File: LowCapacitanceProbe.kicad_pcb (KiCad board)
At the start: 2 copper layers, 23 x 15 mm, 21 parts, among them J1 u.Fl, J5 u.Fl, Q1 BF998, U1 SPX3819M5-L

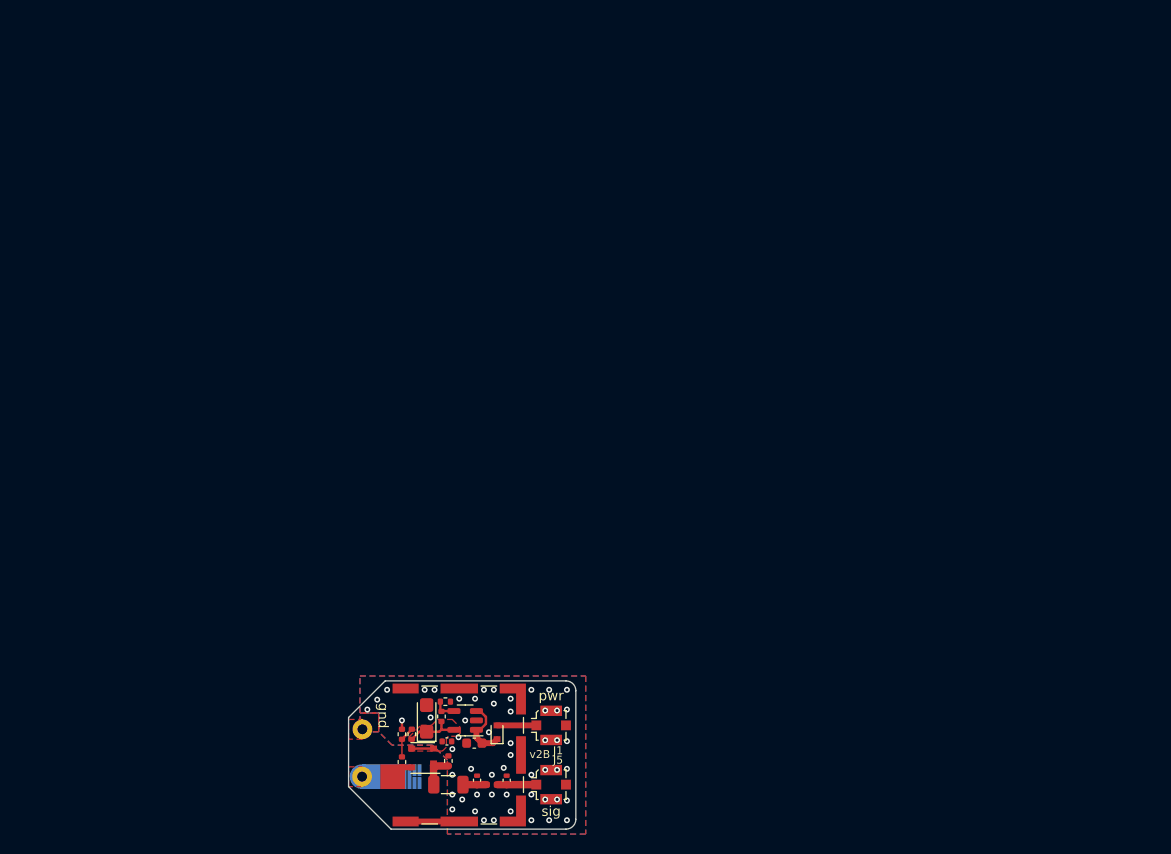
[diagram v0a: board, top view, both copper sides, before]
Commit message: Added net labels, synchronised PCB with SCH, grouped all elements.
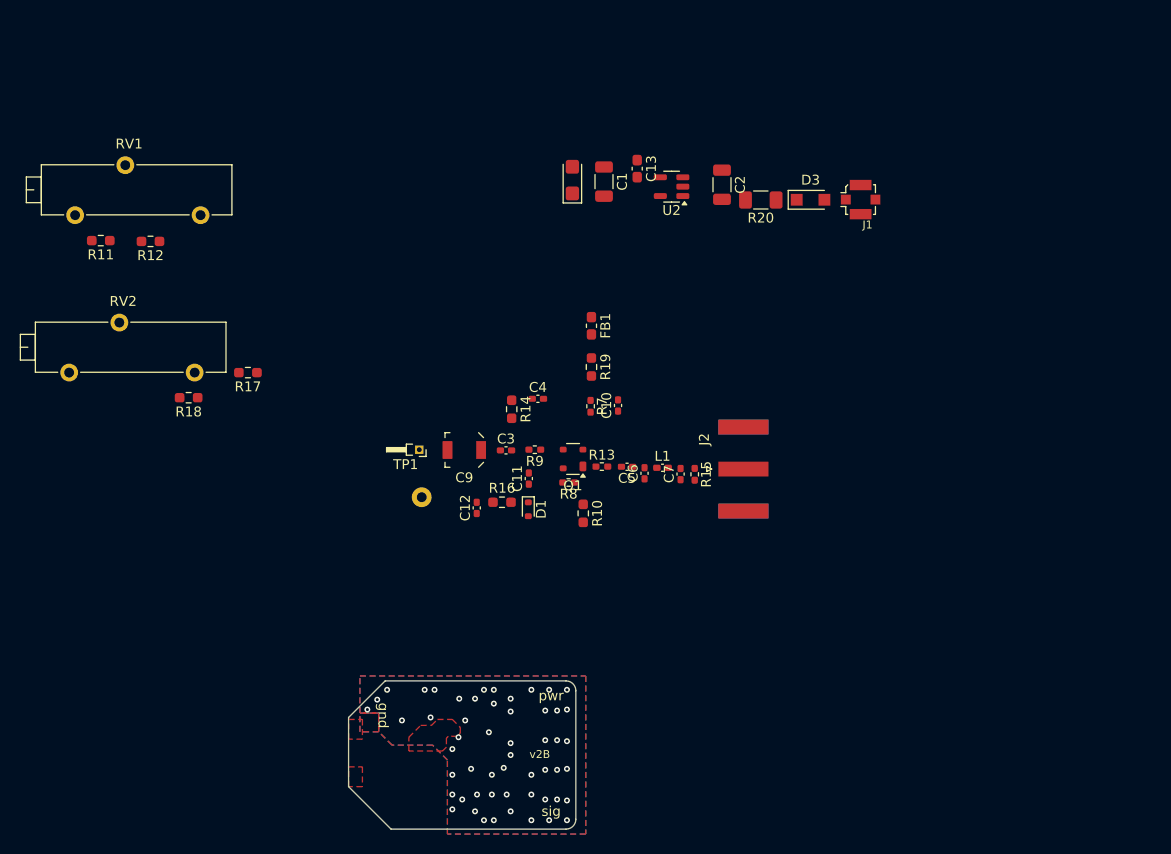
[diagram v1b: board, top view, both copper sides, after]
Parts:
- removed D2: NSR0520V2T1G, Diode_SMD:D_SOD-523
- removed J5: u.Fl, Connector_Coaxial:U.FL_Molex_MCRF_73412-0110_Vertical
- removed N1: Laird_BMI-S-101, RF_Shielding:Laird_Technologies_BMI-S-101_13.66x12.70mm
- removed R1: 4k7, Resistor_SMD:R_0402_1005Metric
- removed R2: 5k6, Resistor_SMD:R_0402_1005Metric
- removed R3: 1M, Resistor_SMD:R_0402_1005Metric
- removed R4: 47R, Resistor_SMD:R_0402_1005Metric
- removed R5: 27k, Resistor_SMD:R_0402_1005Metric
- removed R6: 12k, Resistor_SMD:R_0402_1005Metric
- removed U1: SPX3819M5-L, Package_TO_SOT_SMD:SOT-23-5
- added C10: 100n, Capacitor_SMD:C_0402_1005Metric_Pad0.74x0.62mm_HandSolder, F.Cu at (129.3, 64.6)
- added C11: 3p, Capacitor_SMD:C_0402_1005Metric_Pad0.74x0.62mm_HandSolder, F.Cu at (120.2, 72.0)
- added C12: 100n, Capacitor_SMD:C_0402_1005Metric_Pad0.74x0.62mm_HandSolder, F.Cu at (115.0, 75.0)
- added C13: 100n, Capacitor_SMD:C_0603_1608Metric_Pad1.08x0.95mm_HandSolder, F.Cu at (131.2, 40.7)
- added C3: 3p, Capacitor_SMD:C_0402_1005Metric_Pad0.74x0.62mm_HandSolder, F.Cu at (117.9, 69.2)
- added C9: 1.5-3p, Capacitor_SMD:C_Trimmer_Voltronics_JR, F.Cu at (113.7, 69.1)
- added D1: SMV1232, Diode_SMD:D_SOD-523, F.Cu at (120.2, 75.1)
- added D3: PMEG4020ER, Diode_SMD:Nexperia_CFP3_SOD-123W, F.Cu at (148.8, 43.8)
- added FB1: 0R, Inductor_SMD:L_0603_1608Metric_Pad1.05x0.95mm_HandSolder, F.Cu at (126.6, 56.6)
- added J2: SMA, Connector_Coaxial:SMA_Amphenol_132289_EdgeMount, F.Cu at (142.0, 71.1)
- added R10: 75, Resistor_SMD:R_0603_1608Metric_Pad0.98x0.95mm_HandSolder, F.Cu at (125.8, 75.5)
- added R11: 2k, Resistor_SMD:R_0603_1608Metric_Pad0.98x0.95mm_HandSolder, F.Cu at (76.9, 47.9)
- added R12: 2k, Resistor_SMD:R_0603_1608Metric_Pad0.98x0.95mm_HandSolder, F.Cu at (82.0, 48.0)
- added R13: 0R, Resistor_SMD:R_0402_1005Metric_Pad0.72x0.64mm_HandSolder, F.Cu at (127.6, 70.8)
- added R14: 1M, Resistor_SMD:R_0603_1608Metric_Pad0.98x0.95mm_HandSolder, F.Cu at (118.5, 65.0)
- added R15: 100k, Resistor_SMD:R_0402_1005Metric_Pad0.72x0.64mm_HandSolder, F.Cu at (137.0, 71.6)
- added R16: 1M, Resistor_SMD:R_0603_1608Metric_Pad0.98x0.95mm_HandSolder, F.Cu at (117.5, 74.4)
- added R17: 0R, Resistor_SMD:R_0603_1608Metric_Pad0.98x0.95mm_HandSolder, F.Cu at (91.8, 61.3)
- added R18: 3k, Resistor_SMD:R_0603_1608Metric_Pad0.98x0.95mm_HandSolder, F.Cu at (85.8, 63.8)
- added R19: 0R, Resistor_SMD:R_0603_1608Metric_Pad0.98x0.95mm_HandSolder, F.Cu at (126.6, 60.7)
- added R20: 10, Resistor_SMD:R_1206_3216Metric_Pad1.30x1.75mm_HandSolder, F.Cu at (143.7, 43.8)
- added R7: 10, Resistor_SMD:R_0402_1005Metric_Pad0.72x0.64mm_HandSolder, F.Cu at (126.5, 64.7)
- added R8: 39, Resistor_SMD:R_0402_1005Metric_Pad0.72x0.64mm_HandSolder, F.Cu at (124.3, 72.4)
- added R9: 39, Resistor_SMD:R_0402_1005Metric_Pad0.72x0.64mm_HandSolder, F.Cu at (120.8, 69.1)
- added RV1: 10k, Potentiometer_THT:Potentiometer_Bourns_3006W_Horizontal, F.Cu at (87.0, 45.4)
- added RV2: 10k, Potentiometer_THT:Potentiometer_Bourns_3006W_Horizontal, F.Cu at (86.4, 61.3)
- added TP1: Fixed needle, Connector_PinHeader_1.00mm:PinHeader_1x01_P1.00mm_Horizontal, F.Cu at (109.2, 69.1)
- added U2: SPX3819M5-L-5-0, Package_TO_SOT_SMD:SOT-23-5, F.Cu at (134.7, 42.5)
- C1: footprint Capacitor_SMD:C_0402_1005Metric -> Capacitor_SMD:C_1206_3216Metric
- C2: footprint Capacitor_SMD:C_0603_1608Metric -> Capacitor_SMD:C_1206_3216Metric
- C4: value C -> 100n; footprint FETProbe:input_cap -> Capacitor_SMD:C_0402_1005Metric_Pad0.74x0.62mm_HandSolder
- C5: value 100nF -> 100n; footprint Capacitor_SMD:C_1206_3216Metric -> Capacitor_SMD:C_0402_1005Metric_Pad0.74x0.62mm_HandSolder
- C6, C7: value 2.2pF -> DNP; footprint FETProbe:C_0402_1005Metric_mod -> Capacitor_SMD:C_0402_1005Metric_Pad0.74x0.62mm_HandSolder
- L1: value 10nH -> 4n7; footprint Inductor_SMD:L_0402_1005Metric -> Inductor_SMD:L_0402_1005Metric_Pad0.77x0.64mm_HandSolder
- Q1: footprint FETProbe:SOT-143_mod -> Package_TO_SOT_SMD:SOT-143
- TP3: value TestPoint -> Pogo needle
- moved C2 61.8 mm to (139.8, 42.3), turned to -90 degrees
- moved J1 61.7 mm to (153.8, 43.8)
- moved C1 58.8 mm to (127.8, 42.0), turned to -90 degrees
- moved C8 56.4 mm to (124.7, 41.8)
- moved C4 40.4 mm to (121.2, 64.0)
- moved C5 36.9 mm to (130.2, 70.8), turned to 180 degrees
- moved L1 36.4 mm to (133.8, 70.9)
- moved C7 35.6 mm to (135.6, 71.6), turned to 90 degrees
- moved C6 35.4 mm to (131.9, 71.5), turned to 90 degrees
- moved Q1 33.9 mm to (124.7, 70.0)
- moved TP3 24.2 mm to (109.4, 73.9)
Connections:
- net /out renamed /OUT
- C1 pad 2: 4V0 -> +5V
- C2 pad 2: Net-(D2-K) -> /PIN_FILT
- C4 pad 1: unconnected-(C4-Pad1) -> /G2_BIAS
- C4 pad 2: Net-(Q1-G1) -> GND
- C5 pad 1: /out2 -> /OUT_UNF
- C5 pad 2: /out1 -> Net-(C5-Pad2)
- C6 pad 2: /out1 -> /OUT_UNF
- C8 pad 1: 4V0 -> +5V
- J1 pad 1: Net-(D2-A) -> /PIN
- L1 pad 1: /out1 -> /OUT_UNF
- Q1 pad 1: /out2 -> /SOURCE
- Q1 pad 2: 4V0 -> /DRAIN
- Q1 pad 3: 4V0 -> /G2
- Q1 pad 4: Net-(Q1-G1) -> /G1
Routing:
- net 4V0: track 7.69 -> 0.00 mm
- net Net-(D2-K): track 6.40 -> 0.00 mm
- net GND: track 5.81 -> 0.00 mm
- net Net-(D2-A): track 3.97 -> 0.00 mm
- net /OUT: track 3.92 -> 0.00 mm
- net /out2: track 3.49 -> 0.00 mm
- net Net-(R1-Pad2): track 3.21 -> 0.00 mm
- net /out1: track 2.35 -> 0.00 mm
- net Net-(U1-ADJ): track 2.31 -> 0.00 mm
- net Net-(Q1-G1): track 0.96 -> 0.00 mm
- added copper zone on F.Cu, net (none)
- added copper zone on F.Cu, net +5V
- removed copper zone on F.Cu, net 4V0
- removed copper zone on F.Cu, net unconnected-(C4-Pad1)

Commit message: Slight fixes, simulation modified for varicap analysis and noise analysis, started routing of PCB.
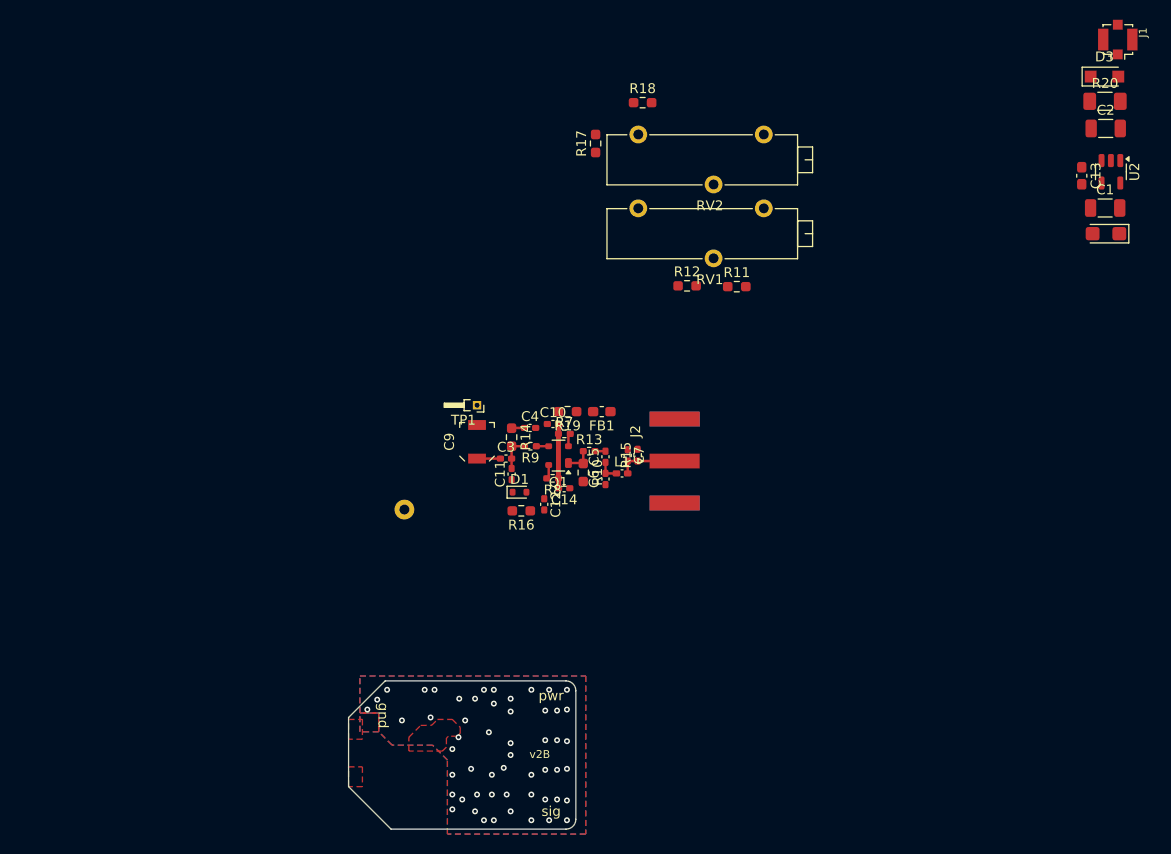
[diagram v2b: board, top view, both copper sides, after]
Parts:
- added C14: 100n, Capacitor_SMD:C_0402_1005Metric_Pad0.74x0.62mm_HandSolder, F.Cu at (123.8, 73.0)
- moved R11 64.5 mm to (141.3, 52.6), turned to 0 degrees
- moved R18 54.8 mm to (131.8, 34.0), turned to 0 degrees
- moved R12 54.5 mm to (136.3, 52.5), turned to 0 degrees
- moved C8 54.3 mm to (178.7, 47.2), turned to 180 degrees
- moved RV2 51.0 mm to (131.3, 37.2), turned to 180 degrees
- moved C1 50.8 mm to (178.6, 44.6), turned to 0 degrees
- moved C13 45.0 mm to (176.2, 41.4)
- moved U2 44.5 mm to (179.2, 41.0), turned to -90 degrees
- moved RV1 44.3 mm to (131.3, 44.7), turned to 180 degrees
- moved R17 42.1 mm to (127.0, 38.1), turned to 90 degrees
- moved C2 39.3 mm to (178.6, 36.6), turned to 0 degrees
- moved R20 36.2 mm to (178.6, 33.8), turned to 0 degrees
- moved D3 32.3 mm to (178.5, 31.3)
- moved J1 30.7 mm to (179.8, 27.6), turned to 0 degrees
- moved FB1 8.75 mm to (127.6, 65.2), turned to 180 degrees
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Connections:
- RV2 pad 3: +5V -> /POWER
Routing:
- net /POWER: track 0.00 -> 6.51 mm
- net /OUT: track 0.00 -> 6.00 mm
- net /IN_2: track 0.00 -> 3.56 mm
- net /SOURCE: track 0.00 -> 2.77 mm
- net Net-(C3-Pad1): track 0.00 -> 2.36 mm
- net /OUT_UNF: track 0.00 -> 2.22 mm
- net /G1: track 0.00 -> 1.43 mm
- net /DRAIN: track 0.00 -> 1.33 mm
- net /G2_BIAS: track 0.00 -> 1.31 mm
- net /G2: track 0.00 -> 1.25 mm
- net Net-(C5-Pad2): track 0.00 -> 1.06 mm

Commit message: Replaced trimmers by smaller SMT types, continued routing.
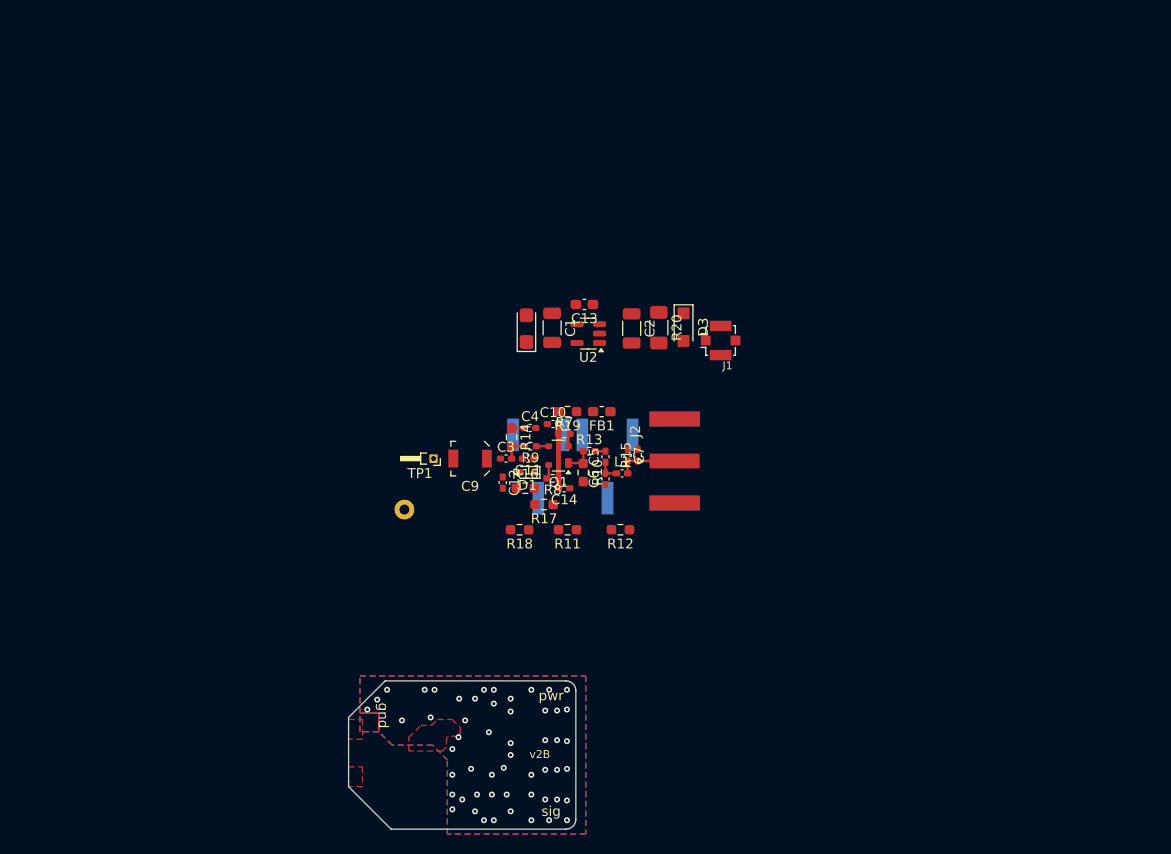
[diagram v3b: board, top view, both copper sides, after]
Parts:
- removed RV1: 10k, Potentiometer_THT:Potentiometer_Bourns_3006W_Horizontal
- added RV3: 10k, Potentiometer_SMD:Potentiometer_Bourns_3269P_Horizontal, B.Cu at (128.2, 70.8)
- RV2: footprint Potentiometer_THT:Potentiometer_Bourns_3006W_Horizontal -> Potentiometer_SMD:Potentiometer_Bourns_3269P_Horizontal; moved to B.Cu
- moved C8 59.4 mm to (120.0, 56.9), turned to 90 degrees
- moved C1 57.3 mm to (122.6, 56.8), turned to -90 degrees
- moved U2 55.4 mm to (126.3, 57.4), turned to 180 degrees
- moved C2 52.1 mm to (130.7, 56.8), turned to -90 degrees
- moved C13 52.0 mm to (125.9, 54.4), turned to 180 degrees
- moved R20 50.6 mm to (133.4, 56.8), turned to -90 degrees
- moved J1 50.4 mm to (139.7, 58.0), turned to -90 degrees
- moved D3 49.6 mm to (135.9, 56.7), turned to -90 degrees
- moved R18 45.0 mm to (119.3, 77.2), turned to 180 degrees
- moved R17 36.9 mm to (121.8, 74.7), turned to 180 degrees
- moved RV2 35.1 mm to (121.2, 70.8), turned to 90 degrees
- moved R11 30.0 mm to (124.2, 77.2), turned to 180 degrees
- moved R12 25.6 mm to (129.5, 77.2), turned to 180 degrees
- moved TP1 6.97 mm to (110.6, 70.0)
- moved C12 4.74 mm to (117.6, 72.4)
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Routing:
- net Net-(C3-Pad1): track 2.36 -> 0.00 mm
- net /IN_2: track 3.56 -> 2.56 mm

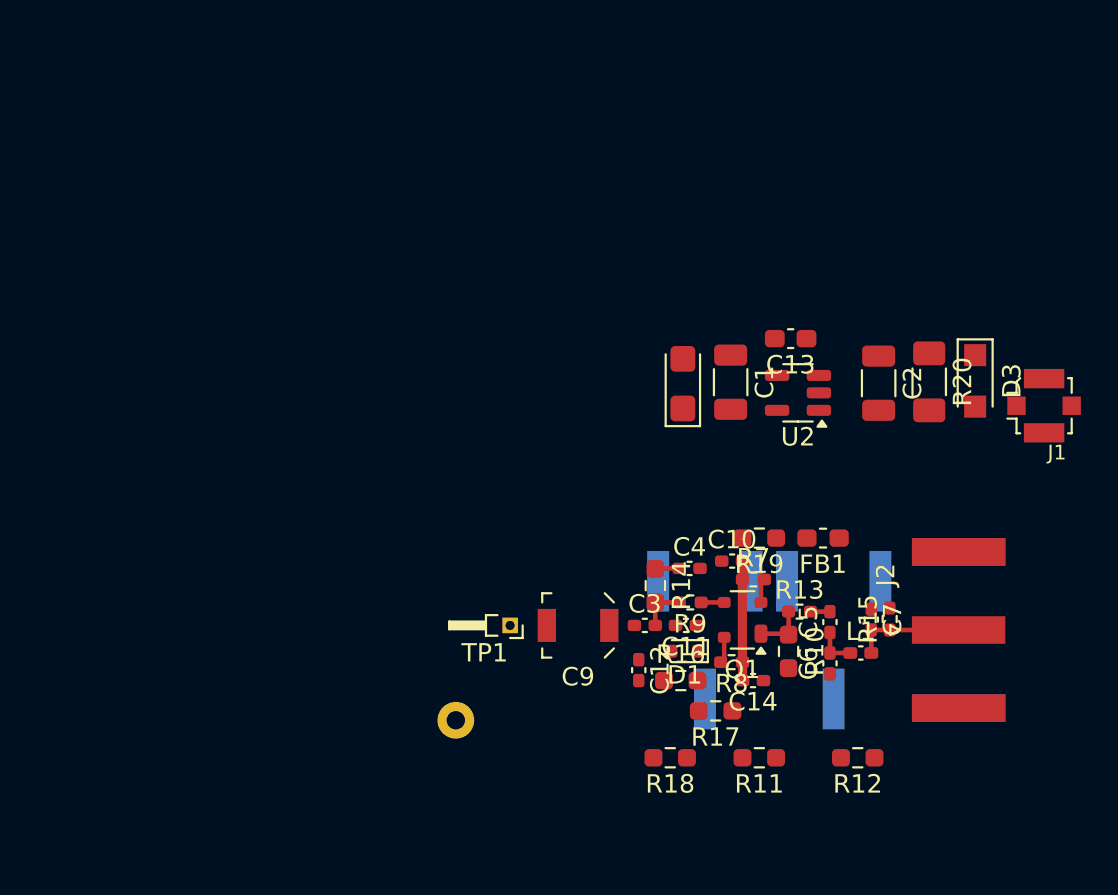
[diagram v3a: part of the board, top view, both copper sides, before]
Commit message: Added mounting point for PCBite holder (M4 nut).
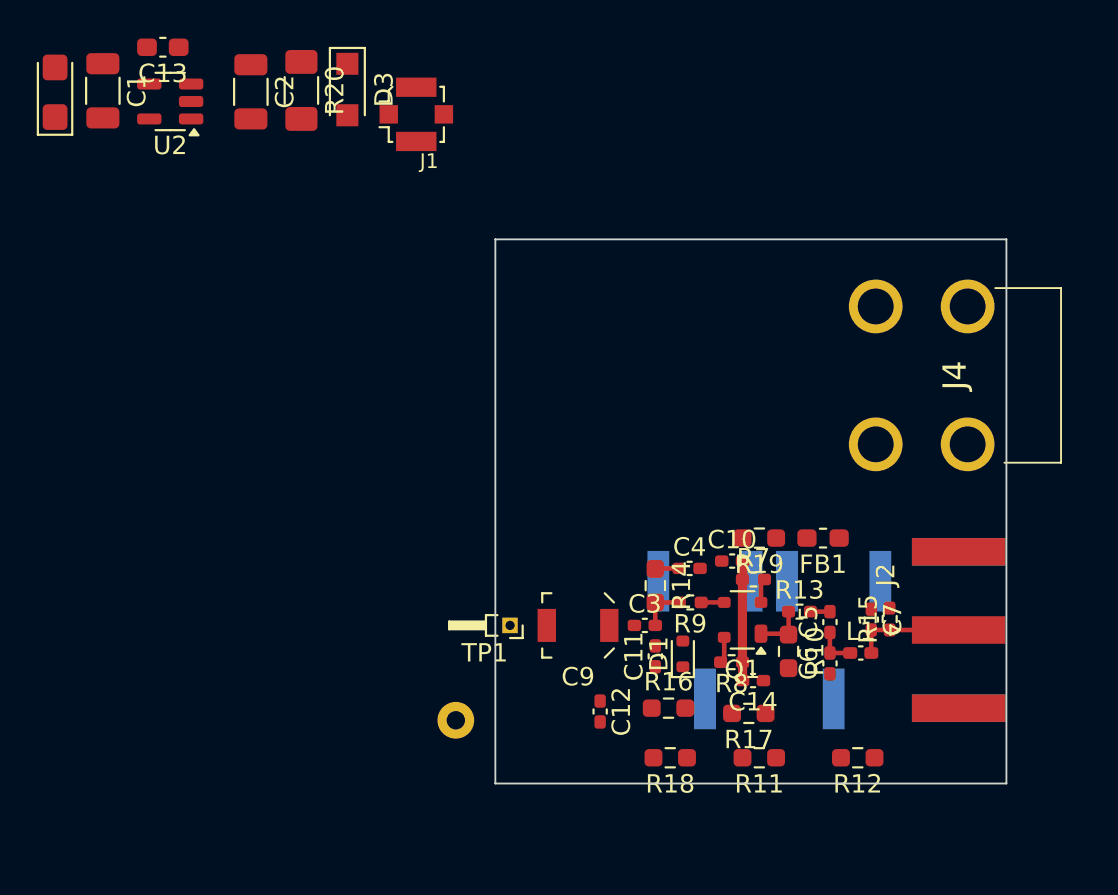
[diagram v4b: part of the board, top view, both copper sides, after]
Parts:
- added J4: 7792, 7792:7792, F.Cu at (130.5, 52.6)
- C13: value 100n -> 100n_LF
- FB1: value 0R -> 0R_FB
- R13: value 0R -> 0
- R20: value 10 -> 10R
- moved C2 37.6 mm to (96.5, 41.0)
- moved C8 37.6 mm to (85.8, 41.0)
- moved D3 37.6 mm to (101.8, 40.9)
- moved R20 37.6 mm to (99.2, 40.9)
- moved U2 37.6 mm to (92.1, 41.5)
- moved J1 37.6 mm to (105.5, 42.2)
- moved C1 37.6 mm to (88.5, 40.9)
- moved C13 37.6 mm to (91.7, 38.5)
- moved C12 3.08 mm to (115.5, 74.7)
- moved C11 2.37 mm to (118.5, 71.7), turned to 90 degrees
- moved R17 1.81 mm to (123.6, 74.8)
- moved R16 1.64 mm to (119.2, 74.5)
- moved D1 0.18 mm to (120.0, 71.5), turned to 90 degrees
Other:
- board size 23 x 15 mm -> 35.6 x 58.5 mm
